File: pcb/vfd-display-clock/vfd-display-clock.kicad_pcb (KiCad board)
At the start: 2 copper layers, 108.5 x 54.6 mm, 34 parts, among them CON1 AVR-ISP-10, IC1 ATTINY26-S, IC2 TD62C950RF, K1 V23079, K2 V23079, P1 CONN_02X05, P2 CONN_01X02, P3 CONN_01X04, P4 CONN_01X04, P5 CONN_01X04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

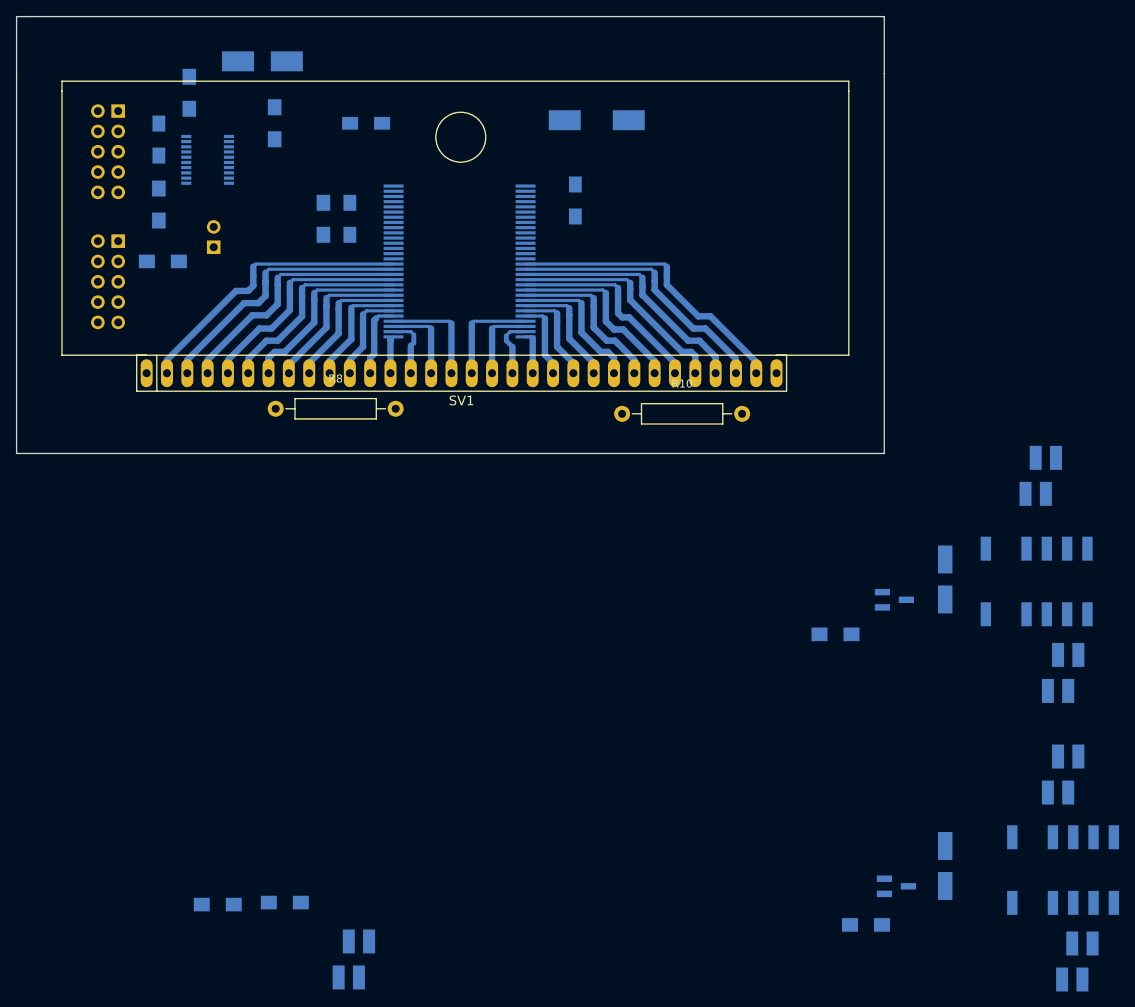
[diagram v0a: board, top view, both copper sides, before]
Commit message: Add receiver library element. Finish clock board.
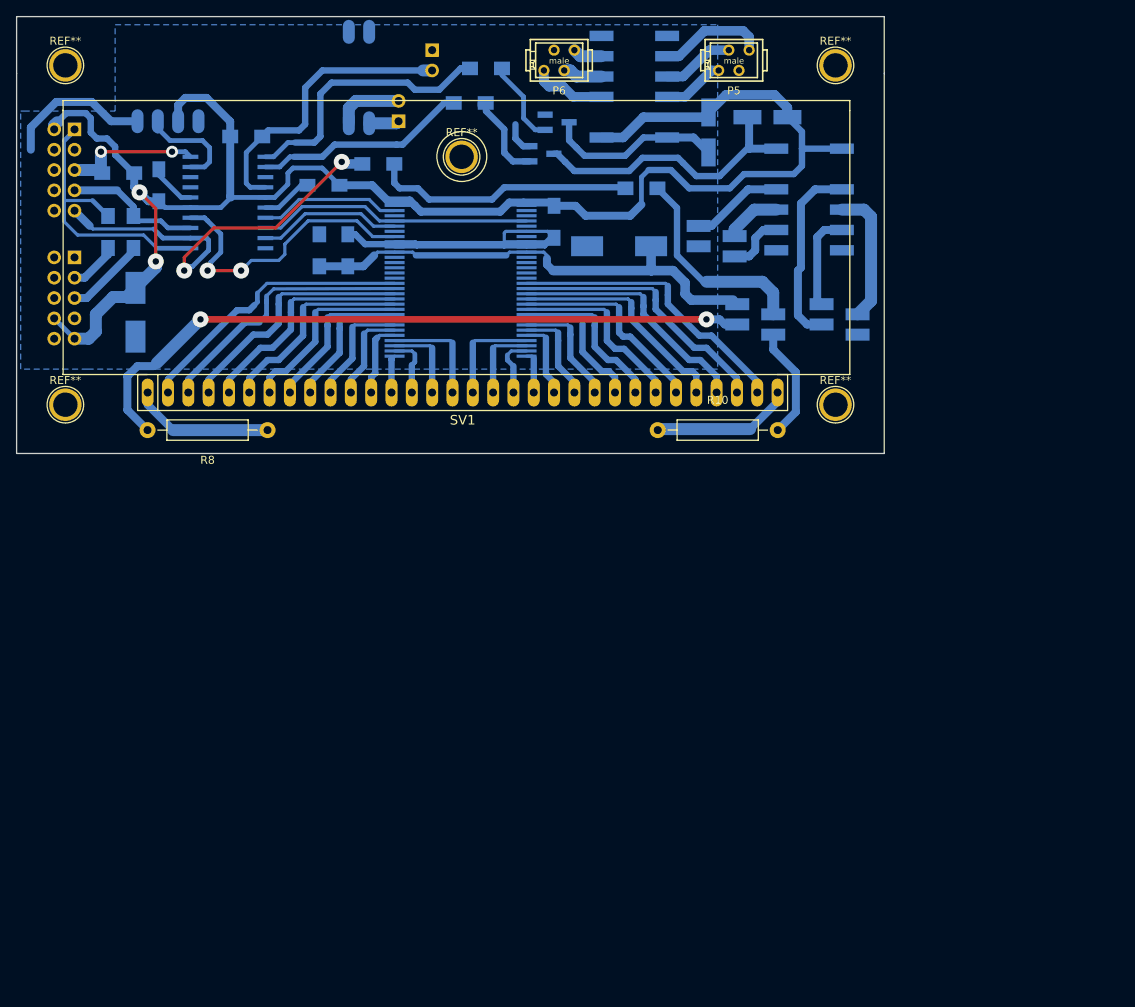
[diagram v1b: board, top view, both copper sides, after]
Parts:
- added IC3: RFM83C-433S, RFM83C_standard:RFM83C_standard, B.Cu at (76.8, 28.8)
- added P8: CONN_01X02, Pin_Headers:Pin_Header_Straight_1x02_Pitch2.54mm, B.Cu at (79.0, 28.8)
- added REF**: 1pin, Connect:1pin, F.Cu at (133.6, 64.3)
- added REF**: 1pin, Connect:1pin, F.Cu at (133.6, 21.8)
- added REF**: 1pin, Connect:1pin, F.Cu at (37.3, 21.8)
- added REF**: 1pin, Connect:1pin, F.Cu at (37.3, 64.3)
- added REF**: 1pin, Connect:1pin, F.Cu at (86.9, 33.3)
- IC1: footprint SMD_Packages:SSOP-20 -> soic:SOIC20
- P5, P6: footprint micro-MaTch:0-188275-4_SMD_4-pin_female -> micro-MaTch:0-215464-4_TH_4-pin_male; moved to F.Cu
- moved P5 120.6 mm to (120.9, 21.2)
- moved R6 117.1 mm to (89.9, 22.2)
- moved K2 111.6 mm to (108.5, 24.5), turned to 90 degrees
- moved P6 109.3 mm to (99.1, 21.2)
- moved Q2 104.5 mm to (98.8, 29.0)
- moved R9 99.8 mm to (109.3, 37.2)
- moved D2 96.4 mm to (117.7, 30.2)
- moved R7 94.7 mm to (76.5, 34.2)
- moved P7 94.4 mm to (123.6, 53.6), turned to 90 degrees
- moved R5 80.6 mm to (87.9, 26.5)
- moved Q1 71.1 mm to (96.9, 32.9)
- moved P3 69.2 mm to (118.7, 43.8), turned to 90 degrees
- moved D1 61.9 mm to (125.1, 28.3), turned to 180 degrees
- moved K1 55.6 mm to (130.3, 38.6), turned to 270 degrees
- moved P2 36.8 mm to (83.2, 19.9), turned to 180 degrees
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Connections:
- CON1 pad 9: /MISO -> /MISO_GAUGE
- IC1 pad 10: (no net) -> /RST
- IC1 pad 11: (no net) -> /REL2
- IC1 pad 12: (no net) -> /REL1
- IC1 pad 14: (no net) -> /1WIRE
- IC1 pad 17: (no net) -> /S-IN
- IC1 pad 18: (no net) -> /CK
- IC1 pad 19: (no net) -> /STB
- IC1 pad 2: /MISO -> /MISO_GAUGE
- IC1 pad 4: (no net) -> /CL
- IC1 pad 9: (no net) -> /RADIO
- IC2 pad 27: (no net) -> /CK
- IC2 pad 32: (no net) -> /S-IN
- IC2 pad 35: (no net) -> /STB
- IC2 pad 37: (no net) -> /CL
- P4 pad 1: Net-(K1-Pad3) -> Net-(K1-Pad5)
- P4 pad 2: (no net) -> Net-(K1-Pad4)
- P4 pad 3: Net-(K1-Pad4) -> Net-(K1-Pad3)
- P4 pad 4: Net-(K1-Pad5) -> (no net)
- P7 pad 1: Net-(P7-Pad1) -> +36V
- P7 pad 3: +36V -> Net-(P7-Pad3)
- R10 pad 2: Net-(P7-Pad1) -> Net-(P7-Pad4)
- R5 pad 1: (no net) -> /REL1
- R6 pad 1: (no net) -> /REL2
- R7 pad 1: (no net) -> /MISO_GAUGE
- R8 pad 2: Net-(P7-Pad2) -> Net-(P7-Pad3)
- R9 pad 2: Net-(P7-Pad4) -> Net-(P7-Pad2)
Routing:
- net +5V: track 0.00 -> 206.8 mm, vias 0 -> 2
- net GND: track 0.00 -> 100.6 mm
- net Net-(P7-Pad3): track 0.00 -> 87.2 mm, vias 0 -> 2
- net +36V: track 0.00 -> 60.6 mm
- net /MISO_GAUGE: track 0.00 -> 52.6 mm, vias 0 -> 2
- net /CL: track 0.00 -> 37.4 mm, vias 0 -> 2
- net /1WIRE: track 0.00 -> 36.6 mm
- net Net-(D1-Pad2): track 0.00 -> 35.9 mm
- net /MOSI_SDA: track 0.00 -> 35.5 mm
- net /CK: track 0.00 -> 34.5 mm
- net /REL2: track 0.00 -> 34.4 mm
- net Net-(R7-Pad2): track 0.00 -> 32.8 mm
- net /REL1: track 0.00 -> 26.9 mm
- net Net-(P7-Pad2): track 0.00 -> 26.1 mm
- net Net-(K1-Pad3): track 0.00 -> 23.4 mm
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- added copper zone on B.Cu, net GND

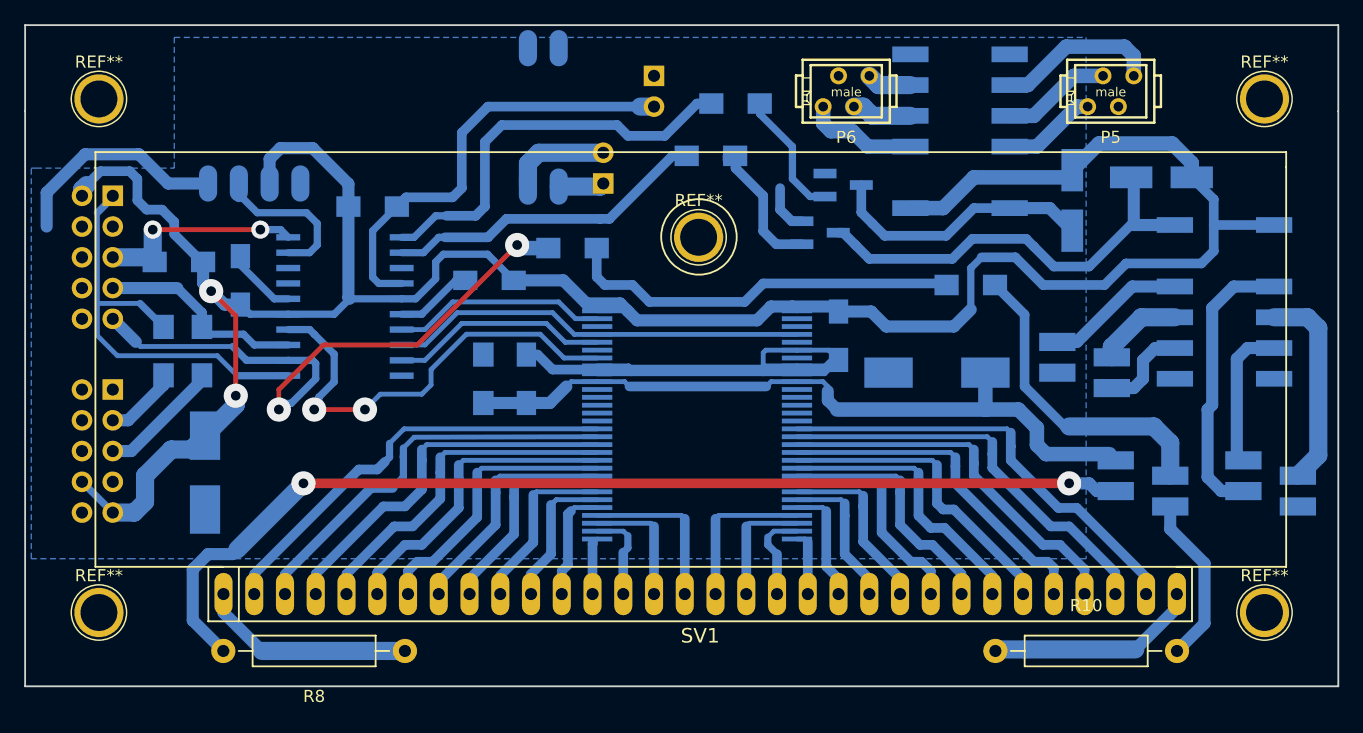
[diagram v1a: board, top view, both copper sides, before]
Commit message: Add symbols, clock board complete.
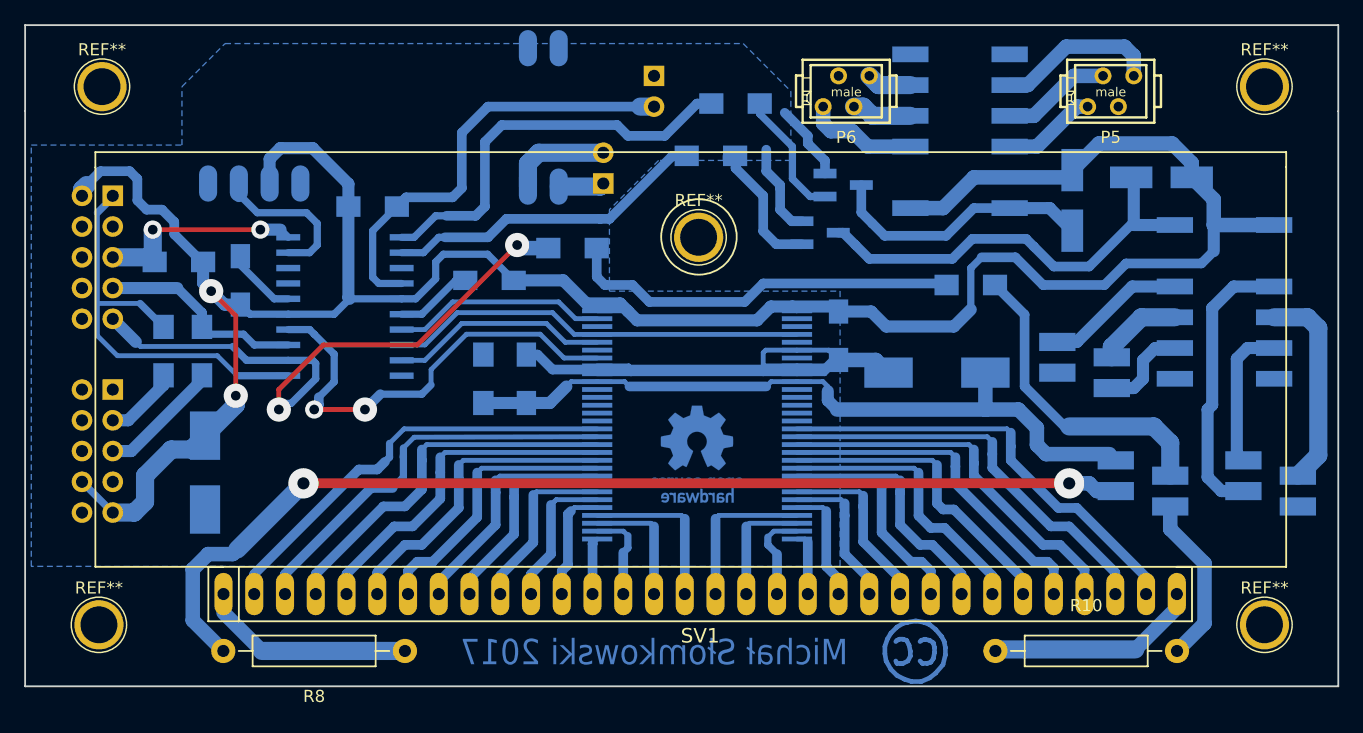
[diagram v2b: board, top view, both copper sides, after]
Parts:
- added REF**: Symbol_CreativeCommons_CopperTop_Type2_Small, Symbols:Symbol_CreativeCommons_CopperTop_Type2_Small, B.Cu at (104.9, 67.6)
- added REF***: OSHW-Logo_7.5x8mm_Copper, Symbols:OSHW-Logo_7.5x8mm_Copper, B.Cu at (86.7, 51.2)
- moved REF** 1.05 mm to (37.6, 20.8)
- moved REF** 1.02 mm to (133.6, 65.3)
- moved REF** 1.02 mm to (37.3, 65.3)
- moved REF** 1.02 mm to (133.6, 20.8)
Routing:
- net GND: track 100.6 -> 96.8 mm
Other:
- rule via_min_size: 0.4 -> 0.8
- board text added: "Michał Słomkowski 2017"
